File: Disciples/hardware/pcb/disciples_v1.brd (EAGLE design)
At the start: 19 x 108.4 mm, 119 parts, among them IC1 OPA1641, IC2 LM324PW, IC3 LM324PW, IC4 TL072D, IC5 LM324PW, IC6 LM4040B10, IC7 LM4040B50, IC8 LM324PW, IC9 LM324PW, J1 PJ301_THONKICONN6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

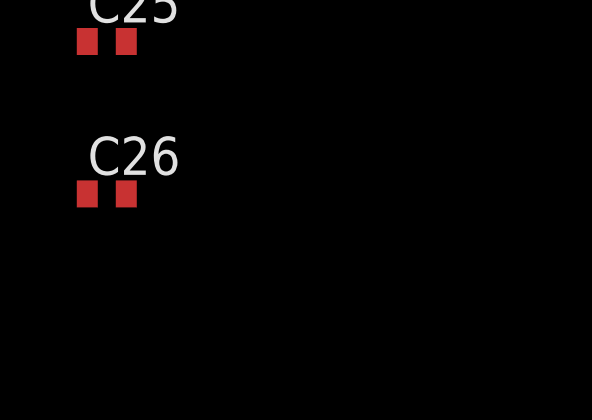
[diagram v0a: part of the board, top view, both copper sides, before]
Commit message: Added stability resistor
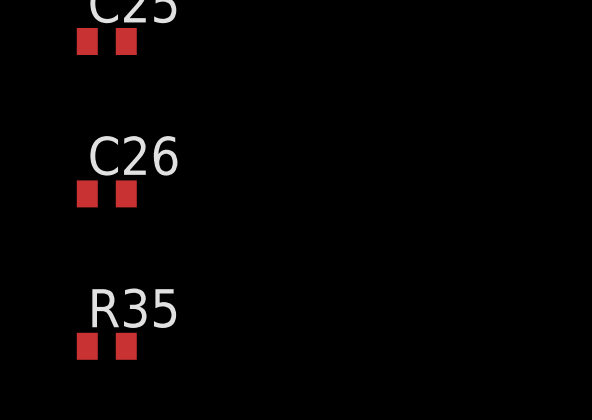
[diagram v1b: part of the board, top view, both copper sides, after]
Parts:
- added R35: 470, rcl:R0402
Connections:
- new net N$55: IC3.8, R28.2, R35.1
- net SLEW: now also R35.2; no longer IC3.8, R28.2
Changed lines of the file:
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@@
 <attribute name="VALUE" x="0" y="-584.5175" size="1.27" layer="27"/>
+</element>
+<element name="R35" library="rcl" package="R0402" value="470" x="0.635" y="-587.6925" smashed="yes">
+<attribute name="NAME" x="0" y="-587.0575" size="1.27" layer="25"/>
+<attribute name="VALUE" x="0" y="-589.5975" size="1.27" layer="27"/>
 </element>
 </elements>
@@
 </signal>
 <signal name="SLEW">
-<contactref element="R28" pad="2"/>
-<contactref element="R2" pad="1"/>
-<contactref element="IC3" pad="8"/>
 <contactref element="J8" pad="P2"/>
 <contactref element="IC5" pad="3"/>
 <contactref element="C11" pad="2"/>
 <contactref element="C10" pad="2"/>
-<wire x1="6.365" y1="-228.2825" x2="1.6025" y2="-223.2025" width="0" layer="19" extent="1-1"/>
+<contactref element="R35" pad="2"/>
+<contactref element="R2" pad="1"/>
 <wire x1="3.81" y1="-341.9475" x2="6.365" y2="-228.2825" width="0" layer="19" extent="1-1"/>
 <wire x1="2.8575" y1="-403.4028" x2="3.81" y2="-341.9475" width="0" layer="19" extent="1-1"/>
 <wire x1="1.285" y1="-532.13" x2="2.8575" y2="-403.4028" width="0" layer="19" extent="1-1"/>
-<wire x1="0.3025" y1="-90.17" x2="1.6025" y2="-223.2025" width="0" layer="19" extent="1-1"/>
-<wire x1="12.2428" y1="10.16" x2="0.3025" y2="-90.17" width="0" layer="19" extent="1-1"/>
+<wire x1="1.285" y1="-587.6925" x2="1.285" y2="-532.13" width="0" layer="19" extent="1-1"/>
+<wire x1="0.3025" y1="-90.17" x2="6.365" y2="-228.2825" width="0" layer="19" extent="1-1"/>
 </signal>
 <signal name="THRESH">
@@
 <wire x1="3.81" y1="-558.4825" x2="1.285" y2="-572.4525" width="0" layer="19" extent="1-1"/>
 </signal>
+<signal name="N$55">
+<contactref element="R28" pad="2"/>
+<contactref element="IC3" pad="8"/>
+<contactref element="R35" pad="1"/>
+<wire x1="12.2428" y1="10.16" x2="1.6025" y2="-223.2025" width="0" layer="19" extent="1-1"/>
+<wire x1="-0.015" y1="-587.6925" x2="1.6025" y2="-223.2025" width="0" layer="19" extent="1-1"/>
+</signal>
 </signals>

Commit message: Forgot a wire
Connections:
- net GND: now also R24.P$1
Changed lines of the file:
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@@
 <contactref element="C26" pad="1"/>
 <contactref element="C25" pad="2"/>
+<contactref element="R24" pad="P$1"/>
 <wire x1="-0.015" y1="-511.81" x2="1.285" y2="-506.73" width="0" layer="19" extent="1-1"/>
 <wire x1="4.1275" y1="-492.8997" x2="1.285" y2="-506.73" width="0" layer="19" extent="1-1"/>
@@
 <wire x1="3.81" y1="-357.505" x2="3.81" y2="-375.6025" width="0" layer="19" extent="1-1"/>
 <wire x1="3.81" y1="-344.4875" x2="3.81" y2="-357.505" width="0" layer="19" extent="1-1"/>
+<wire x1="2.8975" y1="-544.18" x2="-0.015" y2="-511.81" width="0" layer="19" extent="1-1"/>
+<wire x1="3.81" y1="-568.6425" x2="2.8975" y2="-544.18" width="0" layer="19" extent="1-1"/>
+<wire x1="1.285" y1="-577.5325" x2="3.81" y2="-568.6425" width="0" layer="19" extent="1-1"/>
+<wire x1="-0.015" y1="-582.6125" x2="1.285" y2="-577.5325" width="0" layer="19" extent="1-1"/>
 <wire x1="-0.015" y1="-302.5775" x2="3.81" y2="-344.4875" width="0" layer="19" extent="1-1"/>
 <wire x1="1.285" y1="-297.4975" x2="-0.015" y2="-302.5775" width="0" layer="19" extent="1-1"/>
 <wire x1="0.505" y1="-286.7025" x2="1.285" y2="-297.4975" width="0" layer="19" extent="1-1"/>
 <wire x1="3.305" y1="-280.3525" x2="0.505" y2="-286.7025" width="0" layer="19" extent="1-1"/>
-<wire x1="3.81" y1="-568.6425" x2="-0.015" y2="-511.81" width="0" layer="19" extent="1-1"/>
-<wire x1="1.285" y1="-577.5325" x2="3.81" y2="-568.6425" width="0" layer="19" extent="1-1"/>
-<wire x1="-0.015" y1="-582.6125" x2="1.285" y2="-577.5325" width="0" layer="19" extent="1-1"/>
 <wire x1="1.8025" y1="-199.39" x2="3.305" y2="-280.3525" width="0" layer="19" extent="1-1"/>
 <wire x1="2.855" y1="-194.14" x2="1.8025" y2="-199.39" width="0" layer="19" extent="1-1"/>

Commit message: Update disciples_v1.brd
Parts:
- removed U$2: (no value), og-pcb-art:ROHS
- moved R7 0.45 mm to (9.21, 59.7)
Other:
- board text removed: "1V"
- board text removed: "2V"
- board text removed: "4V"
- board text removed: "Attack"
- board text removed: "DC IN"
- board text removed: "DC OUT"
- board text removed: "Detector"
- board text removed: "Ears"
- board text removed: "Envelope"
- board text removed: "Follower"
- board text removed: "Gate"
- board text removed: "Release"
- board text removed: "Threshold"
- board text removed: "cc-by-sa Tom Whitwell, 2014."
- board text removed: "cc-by-sa Émilie Gillet, 2016."
- board text removed: "fast"
- board text removed: "med."
- board text removed: "slow"
- board text removed: "v4"
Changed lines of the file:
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@@
 <wire x1="17.4625" y1="101.7589" x2="17.4625" y2="108.1089" width="0.3048" layer="22"/>
 <wire x1="2.54" y1="108.1089" x2="16.51" y2="108.1089" width="0.1524" layer="22"/>
-<wire x1="10.4775" y1="30.7975" x2="10.4775" y2="21.9075" width="0.1524" layer="22"/>
-<wire x1="10.4775" y1="21.9075" x2="16.8275" y2="21.9075" width="0.1524" layer="22"/>
-<wire x1="16.8275" y1="21.9075" x2="16.8275" y2="30.7975" width="0.1524" layer="22"/>
-<wire x1="16.8275" y1="30.7975" x2="14.9225" y2="30.7975" width="0.1524" layer="22"/>
-<wire x1="14.9225" y1="30.7975" x2="12.3825" y2="30.7975" width="0.1524" layer="22"/>
-<wire x1="12.3825" y1="30.7975" x2="10.4775" y2="30.7975" width="0.1524" layer="22"/>
-<wire x1="2.8575" y1="30.7975" x2="4.7625" y2="30.7975" width="0.1524" layer="22"/>
-<wire x1="4.7625" y1="30.7975" x2="6.6675" y2="30.7975" width="0.1524" layer="22"/>
-<wire x1="6.6675" y1="30.7975" x2="6.6675" y2="21.9075" width="0.1524" layer="22"/>
-<wire x1="6.6675" y1="21.9075" x2="2.8575" y2="21.9075" width="0.1524" layer="22"/>
-<wire x1="2.8575" y1="21.9075" x2="2.8575" y2="30.7975" width="0.1524" layer="22"/>
-<wire x1="12.3825" y1="30.7975" x2="12.3825" y2="32.0675" width="0.1524" layer="22"/>
-<wire x1="14.9225" y1="30.7975" x2="14.9225" y2="32.0675" width="0.1524" layer="22"/>
-<wire x1="4.7625" y1="30.7975" x2="4.7625" y2="32.0675" width="0.1524" layer="22"/>
 <text x="18.2562" y="101.4413" size="1.27" layer="22" ratio="15" rot="MR270">Red stripe</text>
-<text x="17.145" y="1.5875" size="0.635" layer="26" ratio="15" rot="MR0">cc-by-sa Émilie Gillet, 2016.</text>
-<text x="17.1451" y="3.6511" size="3.4" layer="26" ratio="15" rot="MR0">Ears</text>
 <text x="3.0163" y="101.6" size="0.8128" layer="26" ratio="15" rot="MR180">+12V</text>
 <text x="13.1763" y="101.6" size="0.8128" layer="26" ratio="15" rot="MR180">-12V</text>
-<text x="17.145" y="26.67" size="0.8128" layer="22" rot="MR90">med.</text>
-<text x="17.145" y="23.495" size="0.8128" layer="22" rot="MR90">fast</text>
-<text x="18.0975" y="25.0825" size="0.8128" layer="22" rot="MR90">slow</text>
-<text x="2.54" y="25.4" size="0.8128" layer="22" rot="MR270">1V</text>
-<text x="2.54" y="28.575" size="0.8128" layer="22" rot="MR270">2V</text>
-<text x="1.5875" y="26.9875" size="0.8128" layer="22" rot="MR270">4V</text>
-<text x="14.2875" y="32.7025" size="1.016" layer="22" rot="MR90">Attack</text>
-<text x="11.7475" y="32.7025" size="1.016" layer="22" rot="MR90">Release</text>
-<text x="16.51" y="32.7025" size="1.016" layer="22" ratio="15" rot="MR90">Follower</text>
-<text x="6.35" y="32.7025" size="1.016" layer="22" ratio="15" rot="MR90">Detector</text>
-<text x="3.9687" y="32.7025" size="1.016" layer="22" rot="MR90">Threshold</text>
-<text x="17.78" y="32.7025" size="1.016" layer="22" ratio="15" rot="MR90">Envelope</text>
-<text x="7.62" y="32.7025" size="1.016" layer="22" ratio="15" rot="MR90">Gate</text>
-<text x="17.145" y="0.635" size="0.635" layer="26" ratio="15" rot="MR0">cc-by-sa Tom Whitwell, 2014.</text>
 <text x="3.81" y="57.785" size="0.8128" layer="21" ratio="15" rot="R90">+</text>
 <text x="3.81" y="51.435" size="0.8128" layer="21" ratio="15" rot="R90">-</text>
-<text x="17.145" y="2.54" size="0.635" layer="26" ratio="15" rot="MR0">v4</text>
-<text x="3.175" y="66.3575" size="0.8128" layer="51" ratio="15" rot="R90">DC IN</text>
-<text x="17.4625" y="66.3575" size="0.8128" layer="51" ratio="15" rot="R90">DC OUT</text>
 </plain>
 <attributes>
@@
 <attribute name="VALUE" x="10.795" y="16.8275" size="0.4064" layer="27"/>
 </element>
-<element name="U$2" library="og-pcb-art" package="ROHS" value="" x="16.3512" y="61.2775" smashed="yes" rot="MR0"/>
 <element name="J2" library="og-pj301" package="WQP_PJ_301M6" value="PJ301_THONKICONN6" x="14.2875" y="93.98" smashed="yes" rot="R180">
 <attribute name="NAME" x="10.2638" y="98.6625" size="0.8128" layer="25"/>
@@
 <attribute name="VALUE" x="16.9862" y="104.6162" size="0.6096" layer="27" rot="R90"/>
 </element>
-<element name="R7" library="og-pots" package="ALPS_POT_VERTICAL_PS" value="50k" x="9.525" y="60.0075" smashed="yes" rot="R180">
-<attribute name="NAME" x="5.715" y="63.8175" size="1.27" layer="25"/>
-<attribute name="VALUE" x="5.715" y="62.2935" size="1.27" layer="27"/>
+<element name="R7" library="og-pots" package="ALPS_POT_VERTICAL_PS" value="50k" x="9.2075" y="59.69" smashed="yes" rot="R180">
+<attribute name="NAME" x="5.3975" y="63.5" size="1.27" layer="25"/>
+<attribute name="VALUE" x="5.3975" y="61.976" size="1.27" layer="27"/>
 </element>
 <element name="R8" library="rcl" package="R0402" value="510" x="14.605" y="55.5625" smashed="yes" rot="R90">
@@
 <contactref element="C57" pad="2"/>
 <wire x1="3.81" y1="-57.785" x2="18.3125" y2="-182.245" width="0" layer="19" extent="1-1"/>
-<wire x1="7.025" y1="53.0075" x2="3.81" y2="-57.785" width="0" layer="19" extent="1-1"/>
-<wire x1="11.7625" y1="68.2625" x2="7.025" y2="53.0075" width="0" layer="19" extent="1-1"/>
+<wire x1="6.7075" y1="52.69" x2="3.81" y2="-57.785" width="0" layer="19" extent="1-1"/>
+<wire x1="11.7625" y1="68.2625" x2="6.7075" y2="52.69" width="0" layer="19" extent="1-1"/>
 <wire x1="13.5125" y1="70.16" x2="11.7625" y2="68.2625" width="0" layer="19" extent="1-1"/>
 <wire x1="14.9225" y1="70.27" x2="13.5125" y2="70.16" width="0" layer="19" extent="1-1"/>
@@
 <wire x1="10.4625" y1="68.2625" x2="10.4625" y2="66.9925" width="0" layer="19" extent="1-1"/>
 <wire x1="8.7125" y1="70.81" x2="10.4625" y2="68.2625" width="0" layer="19" extent="1-1"/>
-<wire x1="9.525" y1="53.0075" x2="10.4625" y2="66.9925" width="0" layer="19" extent="1-1"/>
+<wire x1="9.2075" y1="52.69" x2="10.4625" y2="66.9925" width="0" layer="19" extent="1-1"/>
 </signal>
 <signal name="N$13">
 <contactref element="R8" pad="1"/>
 <contactref element="R7" pad="P$1"/>
-<wire x1="12.025" y1="53.0075" x2="14.605" y2="54.9125" width="0" layer="19" extent="1-1"/>
+<wire x1="11.7075" y1="52.69" x2="14.605" y2="54.9125" width="0" layer="19" extent="1-1"/>
 </signal>
 <signal name="N$10">
